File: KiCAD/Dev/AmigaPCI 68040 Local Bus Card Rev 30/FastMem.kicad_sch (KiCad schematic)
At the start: 30 parts, among them CN1 SPI, J400 RAMCLK, U400 ICE40HX1K-VQ100, U400F1 W25X20CLSN, U401 SDRAM(16Mx32), U402 SDRAM(16Mx32)

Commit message: Start routing PCLB card, Rev 3.0 08-JUL-2024
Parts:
- removed J400: RAMCLK, Connector_PinHeader_2.54mm:PinHeader_1x03_P2.54mm_Vertical, symbol Connector:Conn_01x03_Pin
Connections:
- net CPUCONF_RST is gone; now on net _CPUCONF: U400.41 (IOB_42_CBSEL0)
- net BCLKA renamed BCLKB
- net PCLKA renamed PCLKB
- no-connect marks 1 -> 8
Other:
- note removed: "RAM CLOCK SPEED"
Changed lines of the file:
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@@
 	(title_block
 		(title "AmigaPCI 68040")
-		(date "2024-07-08")
+		(date "2024-07-09")
 		(rev "3.0")
 	)
@@
 	)
 	(no_connect
+		(at 383.54 158.75)
+	)
+	(no_connect
+		(at 316.23 115.57)
+	)
+	(no_connect
 		(at 377.19 80.01)
 	)
+	(no_connect
+		(at 316.23 95.25)
+	)
+	(no_connect
+		(at 316.23 100.33)
+	)
+	(no_connect
+		(at 316.23 113.03)
+	)
+	(no_connect
+		(at 316.23 97.79)
+	)
+	(no_connect
+		(at 383.54 153.67)
+	)
 	(bus_entry
 		(at 129.54 140.97)
@@
 	(wire
 		(pts
-			(xy 210.439 252.73) (xy 224.79 252.73)
-		)
-		(stroke
-			(width 0)
-			(type default)
-		)
-	)
-	(wire
-		(pts
 			(xy 269.24 49.53) (xy 269.24 55.88)
 		)
@@
 	(wire
 		(pts
-			(xy 210.439 250.19) (xy 224.79 250.19)
-		)
-		(stroke
-			(width 0)
-			(type default)
-		)
-	)
-	(wire
-		(pts
 			(xy 298.45 175.26) (xy 288.29 175.26)
 		)
@@
 	(wire
 		(pts
-			(xy 210.439 247.65) (xy 224.79 247.65)
-		)
-		(stroke
-			(width 0)
-			(type default)
-		)
-	)
-	(wire
-		(pts
 			(xy 55.88 148.59) (xy 73.66 148.59)
 		)
@@
 	)
 	(rectangle
-		(start 193.167 234.442)
-		(end 249.555 257.556)
-		(stroke
-			(width 0)
-			(type default)
-		)
-		(fill
-			(type none)
-		)
-	)
-	(rectangle
 		(start 17.6 17.22)
 		(end 252.2 218.02)
@@
 		)
 	)
-	(text "RAM CLOCK SPEED"
-		(exclude_from_sim no)
-		(at 200.66 241.935 0)
-		(effects
-			(font
-				(size 3 3)
-			)
-			(justify left bottom)
-		)
-	)
 	(text "FAST MEMORY"
 		(exclude_from_sim no)
@@
 		)
 	)
-	(global_label "PCLKA"
+	(global_label "PCLKB"
 		(shape input)
 		(at 384.81 171.45 0)
@@
 		)
 		(property "Intersheetrefs" "${INTERSHEET_REFS}"
-			(at 393.7219 171.45 0)
+			(at 393.9033 171.45 0)
 			(effects
 				(font
@@
 		)
 	)
-	(global_label "CPUCONF_RST"
-		(shape bidirectional)
+	(global_label "_CPUCONF"
+		(shape output)
 		(at 325.12 52.07 180)
 		(fields_autoplaced yes)
@@
 		)
 		(property "Intersheetrefs" "${INTERSHEET_REFS}"
-			(at 307.7187 52.07 0)
+			(at 312.2771 52.07 0)
 			(effects
 				(font
@@
 		)
 	)
-	(global_label "RAMCLK"
-		(shape output)
-		(at 224.79 250.19 0)
-		(fields_autoplaced yes)
-		(effects
-			(font
-				(size 1.27 1.27)
-			)
-			(justify left)
-		)
-		(property "Intersheetrefs" "${INTERSHEET_REFS}"
-			(at 235.1533 250.19 0)
-			(effects
-				(font
-					(size 1.27 1.27)
-				)
-				(justify left)
-			)
-		)
-	)
 	(global_label "_LMBE"
 		(shape input)
@@
 		)
 	)
-	(global_label "PCLK"
-		(shape input)
-		(at 224.79 252.73 0)
-		(fields_autoplaced yes)
-		(effects
-			(font
-				(size 1.27 1.27)
-			)
-			(justify left)
-		)
-		(property "Intersheetrefs" "${INTERSHEET_REFS}"
-			(at 232.6133 252.73 0)
-			(effects
-				(font
-					(size 1.27 1.27)
-				)
-				(justify left)
-			)
-		)
-	)
 	(global_label "BANK1"
 		(shape input)
@@
 		)
 	)
-	(global_label "BCLKA"
+	(global_label "BCLKB"
 		(shape input)
 		(at 384.81 173.99 0)
@@
 		)
 		(property "Intersheetrefs" "${INTERSHEET_REFS}"
-			(at 393.7219 173.99 0)
+			(at 393.9033 173.99 0)
 			(effects
 				(font
@@
 		)
 	)
-	(global_label "BCLK"
-		(shape input)
-		(at 224.79 247.65 0)
-		(fields_autoplaced yes)
-		(effects
-			(font
-				(size 1.27 1.27)
-			)
-			(justify left)
-		)
-		(property "Intersheetrefs" "${INTERSHEET_REFS}"
-			(at 232.6133 247.65 0)
-			(effects
-				(font
-					(size 1.27 1.27)
-				)
-				(justify left)
-			)
-		)
-	)
 	(global_label "_EM1CS"
 		(shape output)
@@
 					(unit 1)
 				)
-			)
-		)
-	)
-	(symbol
-		(lib_id "Connector:Conn_01x03_Pin")
-		(at 205.359 250.19 0)
-		(unit 1)
-		(exclude_from_sim no)
-		(in_bom yes)
-		(on_board yes)
-		(dnp no)
-		(property "Reference" "J400"
-			(at 200.025 248.666 0)
-			(effects
-				(font
-					(size 1.27 1.27)
-				)
-			)
-		)
-		(property "Value" "RAMCLK"
-			(at 200.152 250.698 0)
-			(effects
-				(font
-					(size 1.27 1.27)
-				)
-			)
-		)
-		(property "Footprint" "Connector_PinHeader_2.54mm:PinHeader_1x03_P2.54mm_Vertical"
-			(at 205.359 250.19 0)
-			(effects
-				(font
-					(size 1.27 1.27)
-				)
-				(hide yes)
-			)
-		)
-		(property "Datasheet" "~"
-			(at 205.359 250.19 0)
-			(effects
-				(font
-					(size 1.27 1.27)
-				)
-				(hide yes)
-			)
-		)
-		(property "Description" ""
-			(at 205.359 250.19 0)
-			(effects
-				(font
-					(size 1.27 1.27)
-				)
-				(hide yes)
-			)
-		)
-		(pin "1"
-		)
-		(pin "2"
-		)
-		(pin "3"
-		)
-		(instances
-			(project "AmigaPCI Mainboard"
-				(path "/72453515-27fe-4336-91f3-e3c8054f7767/6050d85a-08ce-47d9-805f-b2a01ec2bdd9"
-					(reference "J400")
-					(unit 1)
-				)
-			)
-			(project "AmigaPCI 68040"
-				(path "/e4eb271a-56d6-4281-ada6-40852f202c68/bb4ae098-973b-46ca-b387-f2229a81b6e3"
-					(reference "J400")
-					(unit 1)
-				)

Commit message: CPU Local Bus Card Rev 3.0 Routing 15-JUL-2024
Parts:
- renumbered CN1 to CN400
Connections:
- net BANK0: now also U400.8 (IOL_3B)
- net BANK1: now also U400.7 (IOL_3A)
- net D3V3B28: no longer U400.15 (IOL_7A_GBIN6), U401.51 (DQ28), U402.51 (DQ28)
- net D3V3B29: no longer U400.16 (IOL_7B), U401.53 (DQ29), U402.53 (DQ29)
- net D3V3B30: no longer U400.19 (IOL_8B), U401.54 (DQ30), U402.54 (DQ30)
- net D3V3B31: no longer U400.18 (IOL_8A), U401.56 (DQ31), U402.56 (DQ31)
- net EMA0: now also U400.86 (IOT_81); no longer U400.95 (IOT_89)
- net EMA1: now also U400.85 (IOT_80); no longer U400.94 (IOT_88)
- net EMA10: now also U400.87 (IOT_82); no longer U400.91 (IOT_86)
- net EMA11: now also U400.89 (IOT_84_GBIN1); no longer U400.90 (IOT_85_GBIN0)
- net EMA12: now also U400.91 (IOT_86); no longer U400.81 (IOT_77)
- net EMA2: now also U400.83 (IOT_79); no longer U400.93 (IOT_87)
- net EMA3: now also U400.100 (IOT_95); no longer U400.96 (IOT_90)
- net EMA4: now also U400.99 (IOT_93); no longer U400.89 (IOT_84_GBIN1)
- net EMA5: now also U400.97 (IOT_91); no longer U400.87 (IOT_82)
- net EMA6: now also U400.96 (IOT_90); no longer U400.86 (IOT_81)
- net EMA7: now also U400.95 (IOT_89); no longer U400.85 (IOT_80)
- net EMA8: now also U400.94 (IOT_88); no longer U400.83 (IOT_79)
- net EMA9: now also U400.93 (IOT_87); no longer U400.82 (IOT_78)
- net EMCLKE: now also U400.2 (IOL_1B); no longer U400.8 (IOL_3B)
- net LVA10: now also U400.73 (IOR_71); no longer U400.80 (IOT_75)
- net LVA11: now also U400.74 (IOR_72); no longer U400.78 (IOT_73)
- net LVA12: now also U400.82 (IOT_78); no longer U400.79 (IOT_74)
- net LVA13: now also U400.59 (IOR_58); no longer U400.74 (IOR_72)
- net LVA14: now also U400.80 (IOT_75); no longer U400.73 (IOR_71)
- net LVA15: now also U400.81 (IOT_77); no longer U400.71 (IOR_69)
- net LVA16: now also U400.15 (IOL_7A_GBIN6); no longer U400.34 (IOB_36_GBIN4)
- net LVA17: now also U400.16 (IOL_7B); no longer U400.36 (IOB_34)
- net LVA18: now also U400.19 (IOL_8B); no longer U400.40 (IOB_41)
- net LVA19: now also U400.18 (IOL_8A); no longer U400.37 (IOB_37)
- net LVA2: now also U400.78 (IOT_73); no longer U400.68 (IOR_67)
- net LVA20: now also U400.20 (IOL_10A); no longer U400.54 (IOR_55)
- net LVA21: now also U400.21 (IOL_10B); no longer U400.53 (IOR_54)
- net LVA22: now also U400.28 (IOB_28); no longer U400.33 (IOB_35_GBIN5)
- net LVA23: now also U400.36 (IOB_34); no longer U400.52 (IOR_53)
- net LVA24: now also U400.24 (IOL_12A); no longer U400.29 (IOB_29)
- net LVA25: now also U400.34 (IOB_36_GBIN4); no longer U400.51 (IOR_52)
- net LVA26: now also U400.29 (IOB_29); no longer U400.30 (IOB_30)
- net LVA27: now also U400.25 (IOL_12B); no longer U400.26 (IOB_26)
- net LVA28: now also U400.30 (IOB_30); no longer U400.28 (IOB_28)
- net LVA29: now also U400.26 (IOB_26); no longer U400.25 (IOL_12B)
- net LVA3: now also U400.79 (IOT_74); no longer U400.66 (IOR_65)
- net LVA30: now also U400.33 (IOB_35_GBIN5); no longer U400.27 (IOB_27)
- net LVA31: now also U400.27 (IOB_27); no longer U400.24 (IOL_12A)
- net LVA5: now also U400.68 (IOR_67); no longer U400.60 (IOR_59)
- net LVA6: now also U400.69 (IOR_68); no longer U400.64 (IOR_63)
- net LVA7: now also U400.71 (IOR_69); no longer U400.57 (IOR_57)
- net LVA8: now also U400.72 (IOR_70); no longer U400.56 (IOR_56)
- net LVA9: now also U400.66 (IOR_65); no longer U400.59 (IOR_58)
- net R_W-3V: now also U400.51 (IOR_52); no longer U400.97 (IOT_91)
- net TT0-3V: now also U400.53 (IOR_54); no longer U400.42 (IOB_43_CBSEL1)
- net _CPUCONF: no longer U400.7 (IOL_3A)
- net _EM0CS: now also U400.9 (IOL_5A); no longer U400.99 (IOT_93)
- net _EM1CS: now also U400.90 (IOT_85_GBIN0); no longer U400.100 (IOT_95)
- net _EMCAS: now also U400.12 (IOL_6A); no longer U400.2 (IOL_1B)
- net _EMRAS: now also U400.10 (IOL_5B); no longer U400.1 (IOL_1A)
- net _EMWE: now also U400.13 (IOL_6B_GBIN7); no longer U400.3 (IOL_2A)
- net _LBEN: now also U400.57 (IOR_57); no longer U400.4 (IOL_2B)
- net _RESET: now also U400.56 (IOR_56); no longer U400.9 (IOL_5A)
- net D3V3B0 renamed D3V3A3
- net D3V3B1 renamed D3V3A0
- net D3V3B10 renamed D3V3A13
- net D3V3B11 renamed D3V3A12
- net D3V3B12 renamed D3V3A11
- net D3V3B13 renamed D3V3A10
- net D3V3B14 renamed D3V3A9
- net D3V3B15 renamed D3V3A8
- net D3V3B16 renamed D3V3A16
- net D3V3B17 renamed D3V3A17
- net D3V3B18 renamed D3V3A18
- net D3V3B19 renamed D3V3A19
- net D3V3B2 renamed D3V3A1
- net D3V3B20 renamed D3V3A20
- net D3V3B21 renamed D3V3A21
- net D3V3B22 renamed D3V3A22
- net D3V3B23 renamed D3V3A23
- net D3V3B24 renamed D3V3A24
- net D3V3B25 renamed D3V3A25
- net D3V3B26 renamed D3V3A26
- net D3V3B27 renamed D3V3A27
- net D3V3B3 renamed D3V3A4
- net D3V3B4 renamed D3V3A2
- net D3V3B5 renamed D3V3A5
- net D3V3B6 renamed D3V3A6
- net D3V3B7 renamed D3V3A7
- net D3V3B8 renamed D3V3A15
- net D3V3B9 renamed D3V3A14
- new net D3V3A28: U401.51 (DQ28), U402.51 (DQ28)
- new net D3V3A29: U401.53 (DQ29), U402.53 (DQ29)
- new net D3V3A30: U401.54 (DQ30), U402.54 (DQ30)
- new net D3V3A31: U401.56 (DQ31), U402.56 (DQ31)
- new net TT1-3V: U400.52 (IOR_53)
- new net _TS-CPU: U400.54 (IOR_55)
- no-connect marks 8 -> 1

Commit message: CPU Local Bus Card routing. 15-JUL-2024
Board is now 6 layers to provide adequate +5V to the 68040.
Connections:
- net _TA-CPU: now also U400.64 (IOR_63)
- net _TS: now reaches U400.60 (IOR_59)
- net _CPUCONF: no longer names the net of U400.41 (IOB_42_CBSEL0)
- net _TS-CPU renamed _TS-3V
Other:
- note removed: "RAMSEY MEMORY LOCATED AT $0700 0000-$07FF FFFF."
- note removed: "Ramsey ID register is at $00DE0043 -04 = $0D -07 = $0F"

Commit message: CPU Local Bus Card Rev 3.0 Routing 18-JUL-2024
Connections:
- no-connect marks 1 -> 8
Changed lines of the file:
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@@
 	(title_block
 		(title "AmigaPCI 68040")
-		(date "2024-07-15")
+		(date "2024-07-18")
 		(rev "3.0")
 	)
@@
 	)
 	(no_connect
+		(at 316.23 82.55)
+	)
+	(no_connect
 		(at 377.19 80.01)
 	)
+	(no_connect
+		(at 325.12 52.07)
+	)
+	(no_connect
+		(at 325.12 54.61)
+	)
+	(no_connect
+		(at 316.23 77.47)
+	)
+	(no_connect
+		(at 316.23 151.13)
+	)
+	(no_connect
+		(at 316.23 85.09)
+	)
+	(no_connect
+		(at 316.23 148.59)
+	)
 	(bus_entry

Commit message: CPU Local Bus Card Rev 3.0 Routing 18-JUL-2024
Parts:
- CN400: footprint Connector_PinHeader_2.54mm:PinHeader_2x03_P2.54mm_Vertical -> Connector_PinHeader_2.54mm:PinHeader_1x06_P2.54mm_Vertical
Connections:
- net BCLKB: now also U400.53 (IOR_54); no longer U400.62 (IOR_60_GBIN3)
- net LVA13: now also U400.64 (IOR_63); no longer U400.59 (IOR_58)
- net PCLKB: now also U400.52 (IOR_53); no longer U400.63 (IOR_61_GBIN2)
- net TT0-3V: now also U400.59 (IOR_58); no longer U400.53 (IOR_54)
- net TT1-3V: now also U400.62 (IOR_60_GBIN3); no longer U400.52 (IOR_53)
- net _LBEN: now also U400.54 (IOR_55); no longer U400.57 (IOR_57)
- net _RESET: now also U400.63 (IOR_61_GBIN2); no longer U400.56 (IOR_56)
- net _TA-CPU: now also U400.56 (IOR_56); no longer U400.64 (IOR_63)
- net _TS-3V: now also U400.57 (IOR_57); no longer U400.54 (IOR_55)
- net _TS: no longer names the net of U400.60 (IOR_59)
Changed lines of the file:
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@@
 	)
 	(label "LVA13"
-		(at 383.54 179.07 180)
+		(at 383.54 168.91 180)
 		(fields_autoplaced yes)
 		(effects
@@
 	(global_label "PCLKB"
 		(shape input)
-		(at 383.54 171.45 0)
+		(at 383.54 191.77 0)
 		(fields_autoplaced yes)
 		(effects
@@
 		)
 		(property "Intersheetrefs" "${INTERSHEET_REFS}"
-			(at 392.6333 171.45 0)
+			(at 392.6333 191.77 0)
 			(effects
 				(font
@@
 	(global_label "_TS-3V"
 		(shape input)
-		(at 383.54 186.69 0)
+		(at 383.54 181.61 0)
 		(fields_autoplaced yes)
 		(effects
@@
 		)
 		(property "Intersheetrefs" "${INTERSHEET_REFS}"
-			(at 393.5404 186.69 0)
+			(at 393.5404 181.61 0)
 			(effects
 				(font
@@
 	(global_label "TT1-3V"
 		(shape input)
-		(at 383.54 191.77 0)
+		(at 383.54 173.99 0)
 		(fields_autoplaced yes)
 		(effects
@@
 		)
 		(property "Intersheetrefs" "${INTERSHEET_REFS}"
-			(at 393.5404 191.77 0)
+			(at 393.5404 173.99 0)
 			(effects
 				(font
@@
 		)
 	)
-	(global_label "_TS"
-		(shape input)
-		(at 383.54 176.53 0)
+	(global_label "BANK1"
+		(shape input)
+		(at 158.75 118.11 180)
+		(fields_autoplaced yes)
+		(effects
+			(font
+				(size 1.27 1.27)
+			)
+			(justify right)
+		)
+		(property "Intersheetrefs" "${INTERSHEET_REFS}"
+			(at 149.5962 118.11 0)
+			(effects
+				(font
+					(size 1.27 1.27)
+				)
+				(justify right)
+			)
+		)
+	)
+	(global_label "TT0-3V"
+		(shape input)
+		(at 383.54 179.07 0)
 		(fields_autoplaced yes)
 		(effects
@@
 		)
 		(property "Intersheetrefs" "${INTERSHEET_REFS}"
-			(at 389.6699 176.53 0)
-			(effects
-				(font
-					(size 1.27 1.27)
-				)
-				(justify left)
-			)
-		)
-	)
-	(global_label "BANK1"
-		(shape input)
-		(at 158.75 118.11 180)
-		(fields_autoplaced yes)
-		(effects
-			(font
-				(size 1.27 1.27)
-			)
-			(justify right)
-		)
-		(property "Intersheetrefs" "${INTERSHEET_REFS}"
-			(at 149.5962 118.11 0)
-			(effects
-				(font
-					(size 1.27 1.27)
-				)
-				(justify right)
-			)
-		)
-	)
-	(global_label "TT0-3V"
-		(shape input)
-		(at 383.54 189.23 0)
-		(fields_autoplaced yes)
-		(effects
-			(font
-				(size 1.27 1.27)
-			)
-			(justify left)
-		)
-		(property "Intersheetrefs" "${INTERSHEET_REFS}"
-			(at 393.5404 189.23 0)
+			(at 393.5404 179.07 0)
 			(effects
 				(font
@@
 	(global_label "BCLKB"
 		(shape input)
-		(at 383.54 173.99 0)
+		(at 383.54 189.23 0)
 		(fields_autoplaced yes)
 		(effects
@@
 		)
 		(property "Intersheetrefs" "${INTERSHEET_REFS}"
-			(at 392.6333 173.99 0)
+			(at 392.6333 189.23 0)
 			(effects
 				(font
@@
 	(global_label "_TA-CPU"
 		(shape output)
-		(at 383.54 168.91 0)
+		(at 383.54 184.15 0)
 		(fields_autoplaced yes)
 		(effects
@@
 		)
 		(property "Intersheetrefs" "${INTERSHEET_REFS}"
-			(at 394.9919 168.91 0)
+			(at 394.9919 184.15 0)
 			(effects
 				(font
@@
 	(global_label "_RESET"
 		(shape input)
-		(at 383.54 184.15 0)
+		(at 383.54 171.45 0)
 		(fields_autoplaced yes)
 		(effects
@@
 		)
 		(property "Intersheetrefs" "${INTERSHEET_REFS}"
-			(at 393.2379 184.15 0)
+			(at 393.2379 171.45 0)
 			(effects
 				(font
@@
 	(global_label "_LBEN"
 		(shape output)
-		(at 383.54 181.61 0)
+		(at 383.54 186.69 0)
 		(fields_autoplaced yes)
 		(effects
@@
 		)
 		(property "Intersheetrefs" "${INTERSHEET_REFS}"
-			(at 392.2704 181.61 0)
+			(at 392.2704 186.69 0)
 			(effects
 				(font
@@
 			)
 		)
-		(property "Footprint" "Connector_PinHeader_2.54mm:PinHeader_2x03_P2.54mm_Vertical"
+		(property "Footprint" "Connector_PinHeader_2.54mm:PinHeader_1x06_P2.54mm_Vertical"
 			(at 262.89 74.93 0)
 			(effects

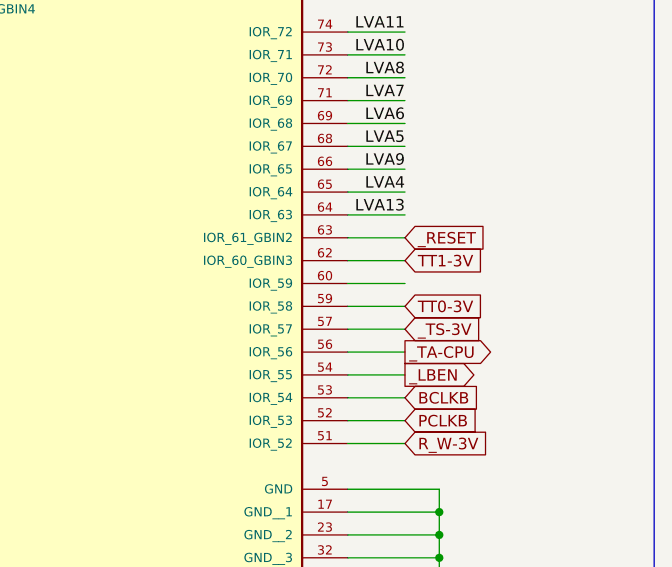
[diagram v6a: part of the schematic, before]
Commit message: CPU Local Bus Card schematics and routing, misc changes to readme's.
This should be project lock for the Rev 3.0 CPU Local Bus Card.
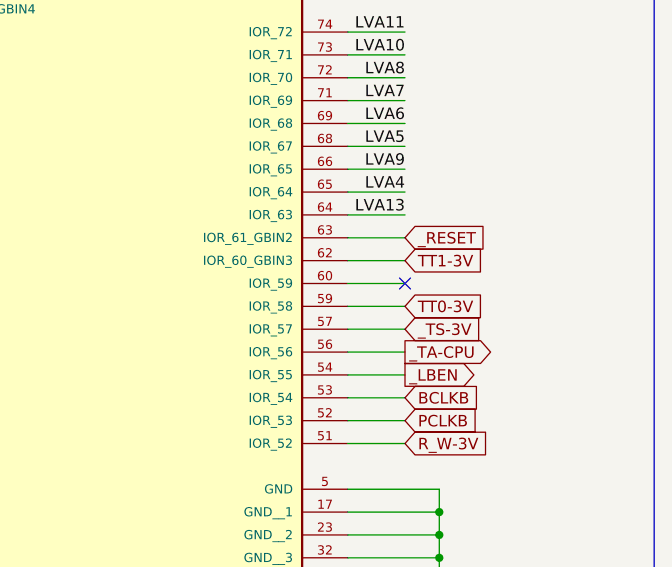
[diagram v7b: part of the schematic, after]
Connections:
- no-connect marks 8 -> 9
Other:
- title: AmigaPCI 68040 -> AmigaPCI 68040 Local Bus Card
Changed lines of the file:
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@@
 	(paper "B")
 	(title_block
-		(title "AmigaPCI 68040")
-		(date "2024-07-18")
+		(title "AmigaPCI 68040 Local Bus Card")
+		(date "2024-07-20")
 		(rev "3.0")
 	)
@@
 	)
 	(no_connect
+		(at 383.54 176.53)
+	)
+	(no_connect
